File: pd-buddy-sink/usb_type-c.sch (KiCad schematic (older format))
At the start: 1 part, among them J2 12401610E4-2A

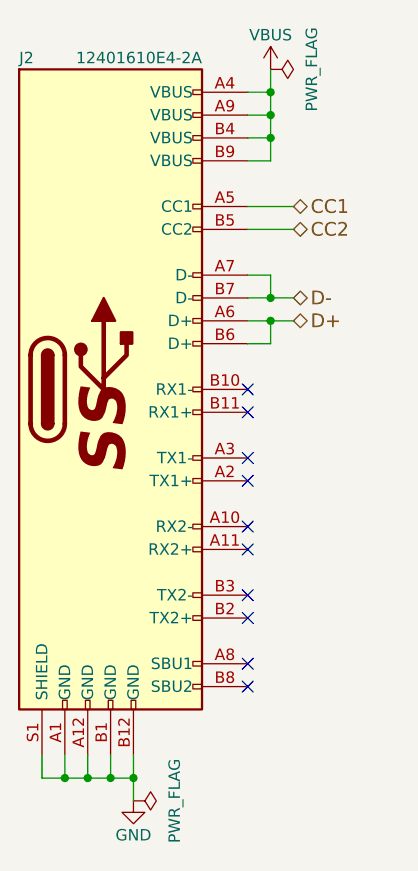
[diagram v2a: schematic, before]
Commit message: Update to KiCad 5.0 nightly
Hooray, new stuff!  The STM32 symbol is a reasonable size now!  We have
a sym-lib-table!  Everything is great, and I'm excited!

The board's a bit of a mess though, as the silkscreen needs to be laid
out nicely.  Oh well, details.
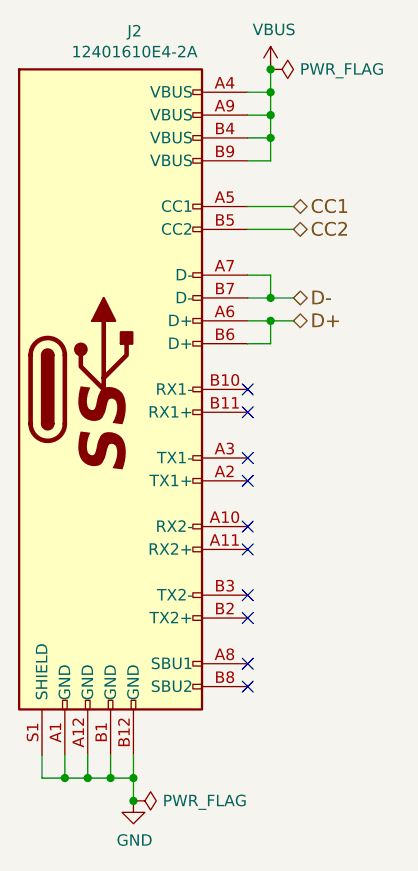
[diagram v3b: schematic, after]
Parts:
- removed J2: 12401610E4-2A, Connectors_USB:USB_C_Receptacle_Amphenol_12401610E4-2A, symbol USB_C_Receptacle
- added J2: 12401610E4-2A, Connector_USB:USB_C_Receptacle_Amphenol_12401610E4-2A, symbol Connector:USB_C_Receptacle
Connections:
- net CC1: now also J2.A5 (CC1)
- net CC2: now also J2.B5 (CC2)
- net D+: now also J2.A6 (D+), J2.B6 (D+)
- net D-: now also J2.A7 (D-), J2.B7 (D-)
- net GND: now also J2.A1 (GND), J2.A12 (GND), J2.B1 (GND), J2.B12 (GND), J2.S1 (SHIELD)
- net VBUS: now also J2.A4 (VBUS), J2.A9 (VBUS), J2.B4 (VBUS), J2.B9 (VBUS)
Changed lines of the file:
@@
-EESchema Schematic File Version 2
-LIBS:power
-LIBS:device
-LIBS:transistors
-LIBS:conn
-LIBS:linear
-LIBS:regul
-LIBS:74xx
-LIBS:cmos4000
-LIBS:adc-dac
-LIBS:memory
-LIBS:xilinx
-LIBS:microcontrollers
-LIBS:dsp
-LIBS:microchip
-LIBS:analog_switches
-LIBS:motorola
-LIBS:texas
-LIBS:intel
-LIBS:audio
-LIBS:interface
-LIBS:digital-audio
-LIBS:philips
-LIBS:display
-LIBS:cypress
-LIBS:siliconi
-LIBS:opto
-LIBS:atmel
-LIBS:contrib
-LIBS:valves
-LIBS:74xgxx
-LIBS:ac-dc
-LIBS:actel
-LIBS:allegro
-LIBS:Altera
-LIBS:analog_devices
-LIBS:battery_management
-LIBS:bbd
-LIBS:brooktre
-LIBS:cmos_ieee
-LIBS:dc-dc
-LIBS:diode
-LIBS:elec-unifil
-LIBS:ESD_Protection
-LIBS:ftdi
-LIBS:gennum
-LIBS:hc11
-LIBS:ir
-LIBS:Lattice
-LIBS:maxim
-LIBS:mechanical
-LIBS:microchip_dspic33dsc
-LIBS:microchip_pic10mcu
-LIBS:microchip_pic12mcu
-LIBS:microchip_pic16mcu
-LIBS:microchip_pic18mcu
-LIBS:microchip_pic32mcu
-LIBS:motor_drivers
-LIBS:motors
-LIBS:msp430
-LIBS:nordicsemi
-LIBS:nxp_armmcu
-LIBS:onsemi
-LIBS:Oscillators
-LIBS:powerint
-LIBS:Power_Management
-LIBS:pspice
-LIBS:references
-LIBS:relays
-LIBS:rfcom
-LIBS:sensors
-LIBS:silabs
-LIBS:stm32
-LIBS:stm8
-LIBS:supertex
-LIBS:switches
-LIBS:transf
-LIBS:ttl_ieee
-LIBS:video
-LIBS:wiznet
-LIBS:Worldsemi
-LIBS:Xicor
-LIBS:zetex
-LIBS:Zilog
-LIBS:pd-buddy
-LIBS:graphic_symbols
+EESchema Schematic File Version 4
 LIBS:pd-buddy-sink-cache
-EELAYER 25 0
+EELAYER 26 0
 EELAYER END
 $Descr USLetter 11000 8500
@@
 Text HLabel 6800 2750 2    60   BiDi ~ 0
 D-
-$Comp
-L USB_C_Receptacle J2
-U 1 1 59147856
-P 6000 3150
-F 0 "J2" H 5600 4600 50  0000 L CNN
-F 1 "12401610E4-2A" H 6400 4600 50  0000 R CNN
-F 2 "Connectors_USB:USB_C_Receptacle_Amphenol_12401610E4-2A" H 6150 3150 50  0001 C CNN
-F 3 "https://www.amphenolcanada.com/StockAvailabilityPrice.aspx?From=&PartNum=12401610E4%7e2A" H 6150 3150 50  0001 C CNN
-	1    6000 3150
-	1    0    0    -1
-$EndComp
 Wire Wire Line
 	6700 2150 6600 2150
 Wire Wire Line
-	6700 1750 6700 2150
+	6700 1750 6700 1850
 Wire Wire Line
 	6600 2050 6700 2050
@@
 	6600 1850 6700 1850
 Connection ~ 6700 1850
-$Comp
-L PWR_FLAG #FLG034
-U 1 1 591479A3
-P 6700 1750
-F 0 "#FLG034" H 6700 1845 50  0001 C CNN
-F 1 "PWR_FLAG" H 6700 1930 50  0000 C CNN
-F 2 "" H 6700 1750 50  0000 C CNN
-F 3 "" H 6700 1750 50  0000 C CNN
-	1    6700 1750
-	0    1    1    0
-$EndComp
 Wire Wire Line
 	6600 2350 6800 2350
@@
 	6800 2450 6600 2450
 Wire Wire Line
-	6600 2750 6800 2750
+	6600 2750 6700 2750
 Wire Wire Line
-	6600 2850 6800 2850
+	6600 2850 6700 2850
 Wire Wire Line
 	6600 2950 6700 2950
@@
 	5700 4750 5700 4850
 Wire Wire Line
-	5700 4850 6100 4850
+	5700 4850 5800 4850
 Wire Wire Line
-	6100 4750 6100 4950
-$Comp
-L GND #PWR035
-U 1 1 59147BA2
-P 6100 4950
-F 0 "#PWR035" H 6100 4700 50  0001 C CNN
-F 1 "GND" H 6100 4800 50  0000 C CNN
-F 2 "" H 6100 4950 50  0000 C CNN
-F 3 "" H 6100 4950 50  0000 C CNN
-	1    6100 4950
-	1    0    0    -1
-$EndComp
-$Comp
-L PWR_FLAG #FLG036
-U 1 1 59147BB3
-P 6100 4950
-F 0 "#FLG036" H 6100 5045 50  0001 C CNN
-F 1 "PWR_FLAG" H 6100 5130 50  0000 C CNN
-F 2 "" H 6100 4950 50  0000 C CNN
-F 3 "" H 6100 4950 50  0000 C CNN
-	1    6100 4950
-	0    1    1    0
-$EndComp
+	6100 4750 6100 4850
 Connection ~ 6100 4850
 Wire Wire Line
@@
 	5800 4750 5800 4850
 Connection ~ 5800 4850
+Wire Wire Line
+	6700 2050 6700 2150
+Wire Wire Line
+	6700 1950 6700 2050
+Wire Wire Line
+	6700 1850 6700 1950
+Wire Wire Line
+	6700 2850 6800 2850
+Wire Wire Line
+	6700 2750 6800 2750
+Wire Wire Line
+	6100 4850 6100 4950
+Wire Wire Line
+	6000 4850 6100 4850
+Wire Wire Line
+	5900 4850 6000 4850
+Wire Wire Line
+	5800 4850 5900 4850
 $Comp
-L VBUS #PWR037
-U 1 1 592B5855
+L Connector:USB_C_Receptacle J2
+U 1 1 5A9A2CD8
+P 6000 3150
+F 0 "J2" H 6105 4717 50  0000 C CNN
+F 1 "12401610E4-2A" H 6105 4626 50  0000 C CNN
+F 2 "Connector_USB:USB_C_Receptacle_Amphenol_12401610E4-2A" H 6150 3150 50  0001 C CNN
+F 3 "http://www.usb.org/developers/docs/usb_31_033017.zip" H 6150 3150 50  0001 C CNN
+	1    6000 3150
+	1    0    0    -1
+$EndComp
+$Comp
+L power:VBUS #PWR0134
+U 1 1 5A9A2E0B
 P 6700 1750
-F 0 "#PWR037" H 6700 1600 50  0001 C CNN
-F 1 "VBUS" H 6700 1900 50  0000 C CNN
+F 0 "#PWR0134" H 6700 1600 50  0001 C CNN
+F 1 "VBUS" H 6715 1923 50  0000 C CNN
 F 2 "" H 6700 1750 50  0001 C CNN
 F 3 "" H 6700 1750 50  0001 C CNN
@@
 	1    0    0    -1
 $EndComp
+$Comp
+L power:PWR_FLAG #FLG0101
+U 1 1 5A9A2ED1
+P 6700 1750
+F 0 "#FLG0101" H 6700 1825 50  0001 C CNN
+F 1 "PWR_FLAG" V 6700 1878 50  0000 L CNN
+F 2 "" H 6700 1750 50  0001 C CNN
+F 3 "" H 6700 1750 50  0001 C CNN
+	1    6700 1750
+	0    1    1    0
+$EndComp
+Connection ~ 6700 1750
+$Comp
+L power:PWR_FLAG #FLG0102
+U 1 1 5A9A2F3E
+P 6100 4950
+F 0 "#FLG0102" H 6100 5025 50  0001 C CNN
+F 1 "PWR_FLAG" V 6100 5078 50  0000 L CNN
+F 2 "" H 6100 4950 50  0001 C CNN
+F 3 "" H 6100 4950 50  0001 C CNN
+	1    6100 4950
+	0    1    1    0
+$EndComp
+$Comp
+L power:GND #PWR0135
+U 1 1 5A9A2FA1
+P 6100 4950
+F 0 "#PWR0135" H 6100 4700 50  0001 C CNN
+F 1 "GND" H 6105 4777 50  0000 C CNN
+F 2 "" H 6100 4950 50  0001 C CNN
+F 3 "" H 6100 4950 50  0001 C CNN
+	1    6100 4950
+	1    0    0    -1
+$EndComp
+Connection ~ 6100 4950
 $EndSCHEMATC
